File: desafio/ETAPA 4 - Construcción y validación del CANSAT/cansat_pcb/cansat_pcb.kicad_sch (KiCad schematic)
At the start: 0 parts

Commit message: update schematic: MPU6050
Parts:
- added C1: 4.7µF, PCM_SparkFun-Semiconductor-Standard:QFN-24-1EP_4x4mm_P0.5mm, symbol Device:C
- added C2, C4, C6: 0.1µF, PCM_SparkFun-Semiconductor-Standard:QFN-24-1EP_4x4mm_P0.5mm, symbol Device:C
- added C3: 0.01µF, PCM_SparkFun-Semiconductor-Standard:QFN-24-1EP_4x4mm_P0.5mm, symbol Device:C
- added C5: 2200pF, PCM_SparkFun-Semiconductor-Standard:QFN-24-1EP_4x4mm_P0.5mm, symbol Device:C
- added C7: 10µF, Package_SO:SOIC-8_3.9x4.9mm_P1.27mm, symbol Device:C_Polarized
- added J1: Conn_01x08_Pin, PCM_SparkFun-Resistor:R_0603_1608Metric, symbol Connector:Conn_01x08_Pin
- added R1: 1kΩ, PCM_SparkFun-Resistor:R_0603_1608Metric, symbol PCM_SparkFun-Resistor:R
- added R2, R3: 2.2kΩ, PCM_SparkFun-Resistor:R_0603_1608Metric, symbol PCM_SparkFun-Resistor:R
- added R4: 4.7kΩ, PCM_SparkFun-Resistor:R_0603_1608Metric, symbol PCM_SparkFun-Resistor:R
- added U1: MPU-6050, PCM_SparkFun-Semiconductor-Standard:QFN-24-1EP_4x4mm_P0.5mm, symbol PCM_SparkFun-Sensor:MPU-6050
- added U2: LP5907MFX-3.3, Package_TO_SOT_SMD:SOT-23-5, symbol Regulator_Linear:LP5907MFX-3.3

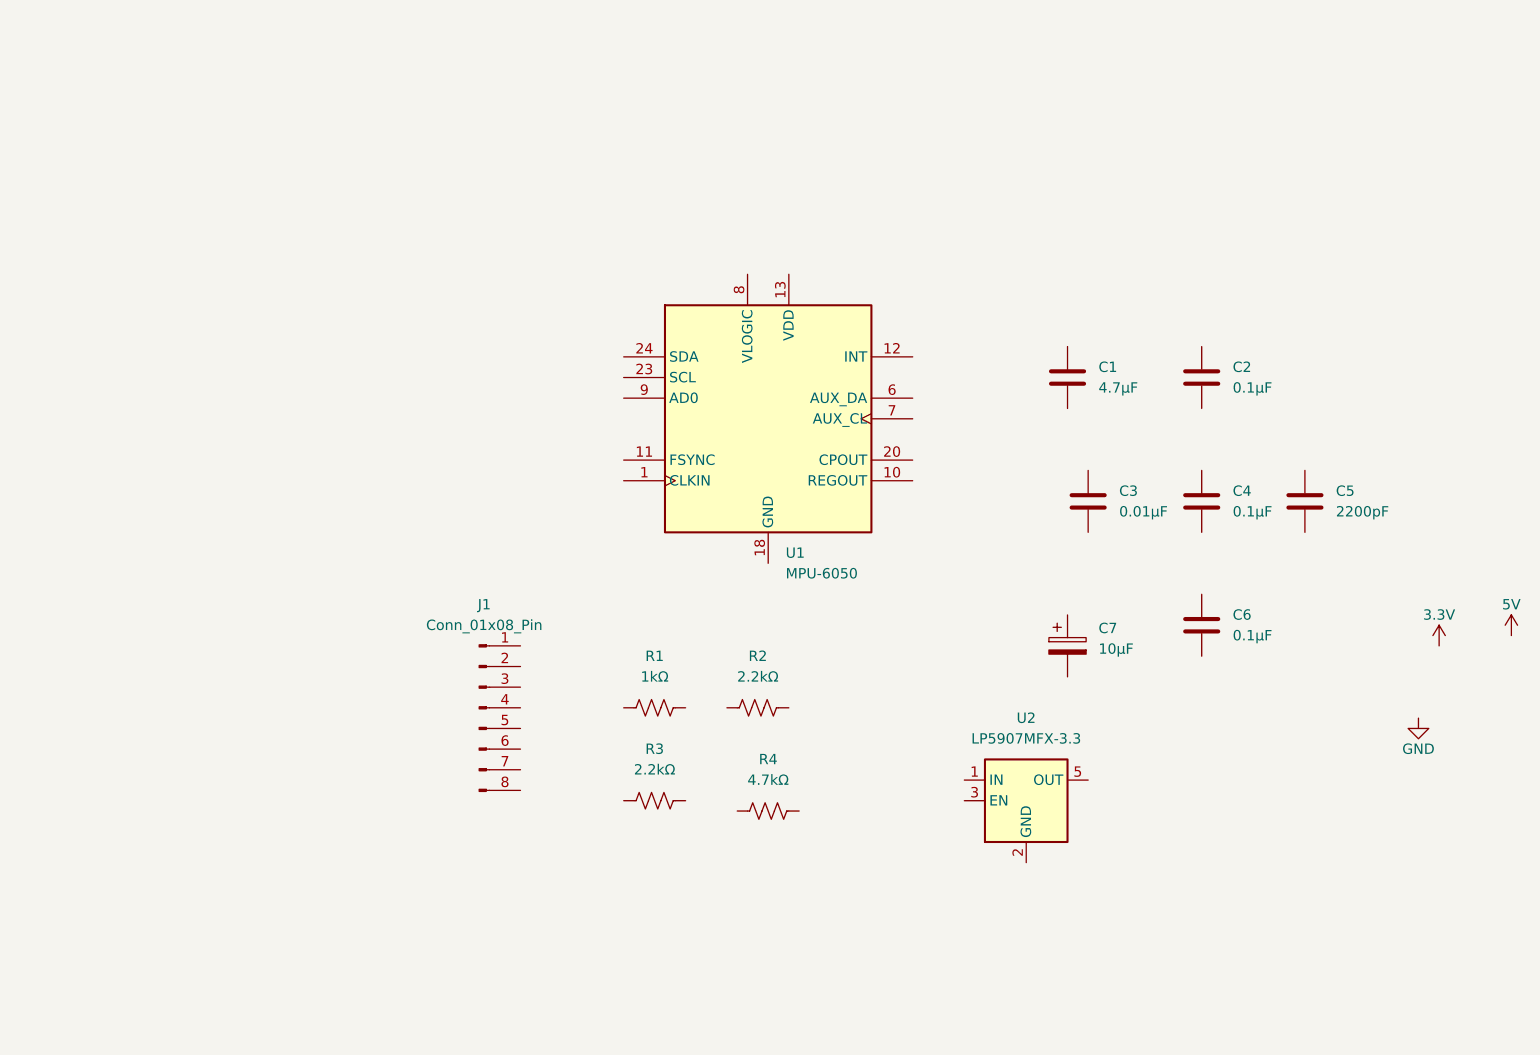
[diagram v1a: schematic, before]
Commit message: update schematic
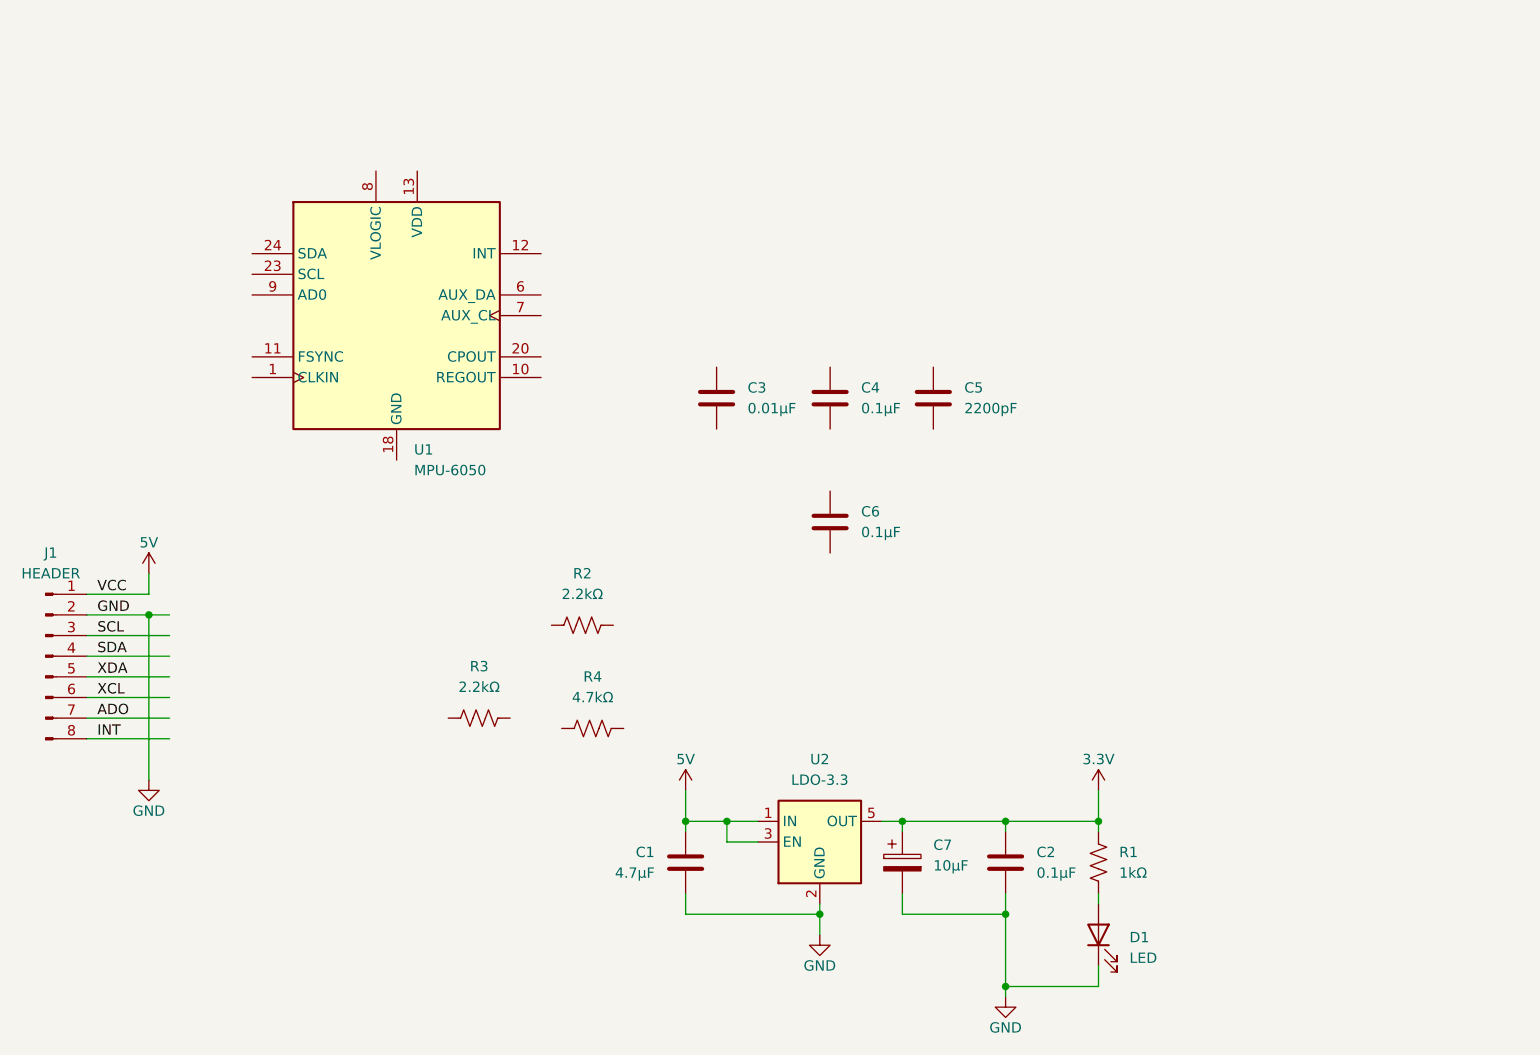
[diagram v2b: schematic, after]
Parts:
- added D1: LED, LED_SMD:LED_Cree-XHP50_3V_HighDensity, symbol Device:LED
- J1: value Conn_01x08_Pin -> HEADER
- U2: value LP5907MFX-3.3 -> LDO-3.3
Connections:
- net 3.3V: now also C2.1, C7.1, R1.1, U2.5 (OUT)
- net 5V: now also C1.1, J1.1 (Pin_1), U2.1 (IN), U2.3 (EN)
- net GND: now also C1.2, C2.2, C7.2, J1.2 (Pin_2), U2.2 (GND), D1.1 (K)
- net at R1.2: now also D1.2 (A)
- net SCL: now reaches J1.3 (Pin_3)
- net SDA: now reaches J1.4 (Pin_4)
- net XDA: now reaches J1.5 (Pin_5)
- net XCL: now reaches J1.6 (Pin_6)
- net ADO: now reaches J1.7 (Pin_7)
- net INT: now reaches J1.8 (Pin_8)
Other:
- moved on the sheet: C1, C2, C3, C4, C5, C6, C7, J1, R1, R2, R3, R4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

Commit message: update pcb
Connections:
- net ADO is gone; now on net AD0: J1.7 (Pin_7)
- net 3.3V: now also C6.1, R2.1, R3.2, U1.13 (VDD)
- net GND: now also C3.2, C4.2, C5.2, C6.2, R4.2, U1.1 (CLKIN), U1.11 (FSYNC), U1.18 (GND)
- net INT: now also U1.12 (INT)
- net SCL: now also R3.1, U1.23 (SCL)
- net SDA: now also R2.2, U1.24 (SDA)
- net XCL: now also U1.7 (AUX_CL)
- net XDA: now also U1.6 (AUX_DA)
- net at U1.10 (REGOUT): now also C4.1
- net at U1.20 (CPOUT): now also C5.1
- net at U1.8 (VLOGIC): now also C3.1
- net AD0: now reaches U1.9 (AD0)
- net AD0: now also R4.1
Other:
- moved on the sheet: C1, C2, C3, C4, C5, C6, C7, D1, J1, R1, R2, R3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
